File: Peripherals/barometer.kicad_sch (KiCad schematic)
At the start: 2 parts, among them U5 MS5637-02BA03

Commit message: Reorganised repo
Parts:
- C18: value 100nF -> (none); footprint Capacitor_SMD:C_0603_1608Metric -> (none)
- U5: value MS5637-02BA03 -> (none); footprint YAR_Sensors:MS5637_1 -> (none)
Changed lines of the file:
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@@
   (symbol (lib_id "power:+3V3") (at 106.68 68.58 0) (unit 1)
     (in_bom yes) (on_board yes) (fields_autoplaced)
-    (property "Reference" "#PWR038" (id 0) (at 106.68 72.39 0)
+    (property "Reference" "#PWR?" (id 0) (at 106.68 72.39 0)
       (effects (font (size 1.27 1.27)) hide)
     )
-    (property "Value" "+3V3" (id 1) (at 106.68 63.5 0))
+    (property "Value" "" (id 1) (at 106.68 63.5 0))
     (property "Footprint" "" (id 2) (at 106.68 68.58 0)
       (effects (font (size 1.27 1.27)) hide)
@@
     (in_bom yes) (on_board yes)
     (property "Reference" "U5" (id 0) (at 129.54 78.74 0))
-    (property "Value" "MS5637-02BA03" (id 1) (at 129.54 81.28 0))
-    (property "Footprint" "YAR_Sensors:MS5637_1" (id 2) (at 127 69.85 0)
+    (property "Value" "" (id 1) (at 129.54 81.28 0))
+    (property "Footprint" "" (id 2) (at 127 69.85 0)
       (effects (font (size 1.27 1.27)) hide)
     )
@@
       (effects (font (size 1.27 1.27)) (justify left))
     )
-    (property "Value" "100nF" (id 1) (at 110.49 82.5499 0)
+    (property "Value" "" (id 1) (at 110.49 82.5499 0)
       (effects (font (size 1.27 1.27)) (justify left))
     )
-    (property "Footprint" "Capacitor_SMD:C_0603_1608Metric" (id 2) (at 107.6452 85.09 0)
+    (property "Footprint" "" (id 2) (at 107.6452 85.09 0)
       (effects (font (size 1.27 1.27)) hide)
     )
@@
   (symbol (lib_id "power:GND") (at 106.68 93.98 0) (unit 1)
     (in_bom yes) (on_board yes) (fields_autoplaced)
-    (property "Reference" "#PWR039" (id 0) (at 106.68 100.33 0)
+    (property "Reference" "#PWR?" (id 0) (at 106.68 100.33 0)
       (effects (font (size 1.27 1.27)) hide)
     )
-    (property "Value" "GND" (id 1) (at 106.68 99.06 0))
+    (property "Value" "" (id 1) (at 106.68 99.06 0))
     (property "Footprint" "" (id 2) (at 106.68 93.98 0)
       (effects (font (size 1.27 1.27)) hide)

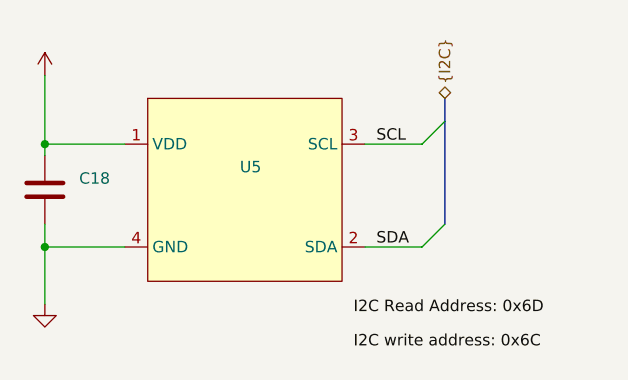
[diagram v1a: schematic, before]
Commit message: rev2 changes excluding pyro
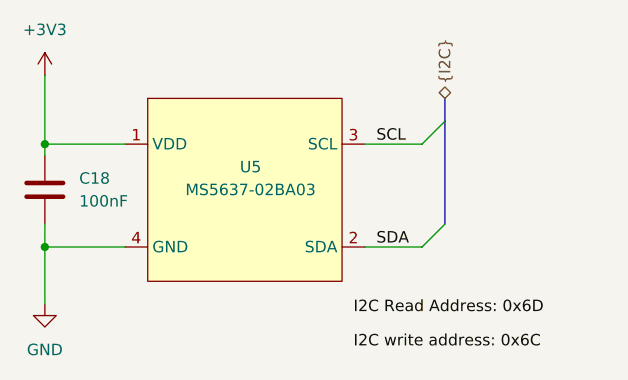
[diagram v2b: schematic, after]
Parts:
- C18: value (none) -> 100nF; footprint (none) -> Capacitor_SMD:C_0603_1608Metric
- U5: value (none) -> MS5637-02BA03; footprint (none) -> YAR_Sensors:MS5637_1
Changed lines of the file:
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@@
-(kicad_sch (version 20211123) (generator eeschema)
+(kicad_sch (version 20230121) (generator eeschema)
   (paper "A5")
   (title_block
@@
   )
   (bus_entry (at 151.13 85.09) (size -2.54 2.54)
-    (stroke (width 0) (type default) (color 0 0 0 0))
+    (stroke (width 0) (type default))
   )
   (bus_entry (at 151.13 73.66) (size -2.54 2.54)
-    (stroke (width 0) (type default) (color 0 0 0 0))
+    (stroke (width 0) (type default))
   )
   (wire (pts (xy 142.24 76.2) (xy 148.59 76.2))
-    (stroke (width 0) (type default) (color 0 0 0 0))
+    (stroke (width 0) (type default))
   )
   (wire (pts (xy 115.57 87.63) (xy 106.68 87.63))
-    (stroke (width 0) (type default) (color 0 0 0 0))
+    (stroke (width 0) (type default))
   )
   (wire (pts (xy 106.68 87.63) (xy 106.68 93.98))
-    (stroke (width 0) (type default) (color 0 0 0 0))
+    (stroke (width 0) (type default))
   )
   (bus (pts (xy 151.13 73.66) (xy 151.13 85.09))
-    (stroke (width 0) (type default) (color 0 0 0 0))
+    (stroke (width 0) (type default))
   )
   (wire (pts (xy 142.24 87.63) (xy 148.59 87.63))
-    (stroke (width 0) (type default) (color 0 0 0 0))
+    (stroke (width 0) (type default))
   )
   (bus (pts (xy 151.13 71.12) (xy 151.13 73.66))
-    (stroke (width 0) (type default) (color 0 0 0 0))
+    (stroke (width 0) (type default))
   )
   (wire (pts (xy 115.57 76.2) (xy 106.68 76.2))
-    (stroke (width 0) (type default) (color 0 0 0 0))
+    (stroke (width 0) (type default))
   )
   (wire (pts (xy 106.68 85.09) (xy 106.68 87.63))
-    (stroke (width 0) (type default) (color 0 0 0 0))
+    (stroke (width 0) (type default))
   )
   (wire (pts (xy 106.68 76.2) (xy 106.68 77.47))
-    (stroke (width 0) (type default) (color 0 0 0 0))
+    (stroke (width 0) (type default))
   )
   (wire (pts (xy 106.68 76.2) (xy 106.68 68.58))
-    (stroke (width 0) (type default) (color 0 0 0 0))
+    (stroke (width 0) (type default))
   )
-  (label "SCL" (at 143.51 76.2 0)
+  (label "SCL" (at 143.51 76.2 0) (fields_autoplaced)
     (effects (font (size 1.27 1.27)) (justify left bottom))
   )
-  (label "I2C write address: 0x6C" (at 140.97 99.06 0)
+  (label "I2C write address: 0x6C" (at 140.97 99.06 0) (fields_autoplaced)
     (effects (font (size 1.27 1.27)) (justify left bottom))
   )
-  (label "SDA" (at 143.51 87.63 0)
+  (label "SDA" (at 143.51 87.63 0) (fields_autoplaced)
     (effects (font (size 1.27 1.27)) (justify left bottom))
   )
-  (label "I2C Read Address: 0x6D" (at 140.97 95.25 0)
+  (label "I2C Read Address: 0x6D" (at 140.97 95.25 0) (fields_autoplaced)
     (effects (font (size 1.27 1.27)) (justify left bottom))
   )
-  (hierarchical_label "{I2C}" (shape bidirectional) (at 151.13 71.12 90)
+  (hierarchical_label "{I2C}" (shape bidirectional) (at 151.13 71.12 90) (fields_autoplaced)
     (effects (font (size 1.27 1.27)) (justify left))
   )
   (symbol (lib_id "power:+3V3") (at 106.68 68.58 0) (unit 1)
-    (in_bom yes) (on_board yes) (fields_autoplaced)
-    (property "Reference" "#PWR?" (id 0) (at 106.68 72.39 0)
+    (in_bom yes) (on_board yes) (dnp no) (fields_autoplaced)
+    (property "Reference" "#PWR038" (at 106.68 72.39 0)
       (effects (font (size 1.27 1.27)) hide)
     )
-    (property "Value" "" (id 1) (at 106.68 63.5 0))
-    (property "Footprint" "" (id 2) (at 106.68 68.58 0)
+    (property "Value" "+3V3" (at 106.68 63.5 0)
+      (effects (font (size 1.27 1.27)))
+    )
+    (property "Footprint" "" (at 106.68 68.58 0)
       (effects (font (size 1.27 1.27)) hide)
     )
-    (property "Datasheet" "" (id 3) (at 106.68 68.58 0)
+    (property "Datasheet" "" (at 106.68 68.58 0)
       (effects (font (size 1.27 1.27)) hide)
     )
     (pin "1")
+    (instances
+      (project "Phoenix"
+        (path "/c01d5cd9-eb44-4300-834c-2f034f7de019/094703ac-bbe4-46f1-9755-0d9526f1d0ba"
+          (reference "#PWR038") (unit 1)
+        )
+      )
+    )
   )
   (symbol (lib_id "Sensor:MS5637-02BA03") (at 127 69.85 0) (unit 1)
-    (in_bom yes) (on_board yes)
-    (property "Reference" "U5" (id 0) (at 129.54 78.74 0))
-    (property "Value" "" (id 1) (at 129.54 81.28 0))
-    (property "Footprint" "" (id 2) (at 127 69.85 0)
+    (in_bom yes) (on_board yes) (dnp no)
+    (property "Reference" "U5" (at 129.54 78.74 0)
+      (effects (font (size 1.27 1.27)))
+    )
+    (property "Value" "MS5637-02BA03" (at 129.54 81.28 0)
+      (effects (font (size 1.27 1.27)))
+    )
+    (property "Footprint" "YAR_Sensors:MS5637_1" (at 127 69.85 0)
       (effects (font (size 1.27 1.27)) hide)
     )
-    (property "Datasheet" "" (id 3) (at 127 69.85 0)
+    (property "Datasheet" "" (at 127 69.85 0)
       (effects (font (size 1.27 1.27)) hide)
     )
@@
     (pin "3")
     (pin "4")
+    (instances
+      (project "Phoenix"
+        (path "/c01d5cd9-eb44-4300-834c-2f034f7de019/094703ac-bbe4-46f1-9755-0d9526f1d0ba"
+          (reference "U5") (unit 1)
+        )
+      )
+    )
   )
   (symbol (lib_id "Device:C") (at 106.68 81.28 0) (unit 1)
-    (in_bom yes) (on_board yes) (fields_autoplaced)
-    (property "Reference" "C18" (id 0) (at 110.49 80.0099 0)
+    (in_bom yes) (on_board yes) (dnp no) (fields_autoplaced)
+    (property "Reference" "C18" (at 110.49 80.0099 0)
       (effects (font (size 1.27 1.27)) (justify left))
     )
-    (property "Value" "" (id 1) (at 110.49 82.5499 0)
+    (property "Value" "100nF" (at 110.49 82.5499 0)
       (effects (font (size 1.27 1.27)) (justify left))
     )
-    (property "Footprint" "" (id 2) (at 107.6452 85.09 0)
+    (property "Footprint" "Capacitor_SMD:C_0603_1608Metric" (at 107.6452 85.09 0)
       (effects (font (size 1.27 1.27)) hide)
     )
-    (property "Datasheet" "~" (id 3) (at 106.68 81.28 0)
+    (property "Datasheet" "~" (at 106.68 81.28 0)
       (effects (font (size 1.27 1.27)) hide)
     )
     (pin "1")
     (pin "2")
+    (instances
+      (project "Phoenix"
+        (path "/c01d5cd9-eb44-4300-834c-2f034f7de019/094703ac-bbe4-46f1-9755-0d9526f1d0ba"
+          (reference "C18") (unit 1)
+        )
+      )
+    )
   )
   (symbol (lib_id "power:GND") (at 106.68 93.98 0) (unit 1)
-    (in_bom yes) (on_board yes) (fields_autoplaced)
-    (property "Reference" "#PWR?" (id 0) (at 106.68 100.33 0)
+    (in_bom yes) (on_board yes) (dnp no) (fields_autoplaced)
+    (property "Reference" "#PWR039" (at 106.68 100.33 0)
       (effects (font (size 1.27 1.27)) hide)
     )
-    (property "Value" "" (id 1) (at 106.68 99.06 0))
-    (property "Footprint" "" (id 2) (at 106.68 93.98 0)
+    (property "Value" "GND" (at 106.68 99.06 0)
+      (effects (font (size 1.27 1.27)))
+    )
+    (property "Footprint" "" (at 106.68 93.98 0)
       (effects (font (size 1.27 1.27)) hide)
     )
-    (property "Datasheet" "" (id 3) (at 106.68 93.98 0)
+    (property "Datasheet" "" (at 106.68 93.98 0)
       (effects (font (size 1.27 1.27)) hide)
     )
     (pin "1")
+    (instances
+      (project "Phoenix"
+        (path "/c01d5cd9-eb44-4300-834c-2f034f7de019/094703ac-bbe4-46f1-9755-0d9526f1d0ba"
+          (reference "#PWR039") (unit 1)
+        )
+      )
+    )
   )
 )
